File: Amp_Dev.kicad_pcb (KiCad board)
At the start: 2 copper layers, 100 x 100 mm, 39 parts, among them J1 SMA, J10 SMA, J11 CONN_01X02, Q1 DMN2075U, U1 MML09211H, U4 SN74LVC1G17, U5 TLV702, U6 LTC2644

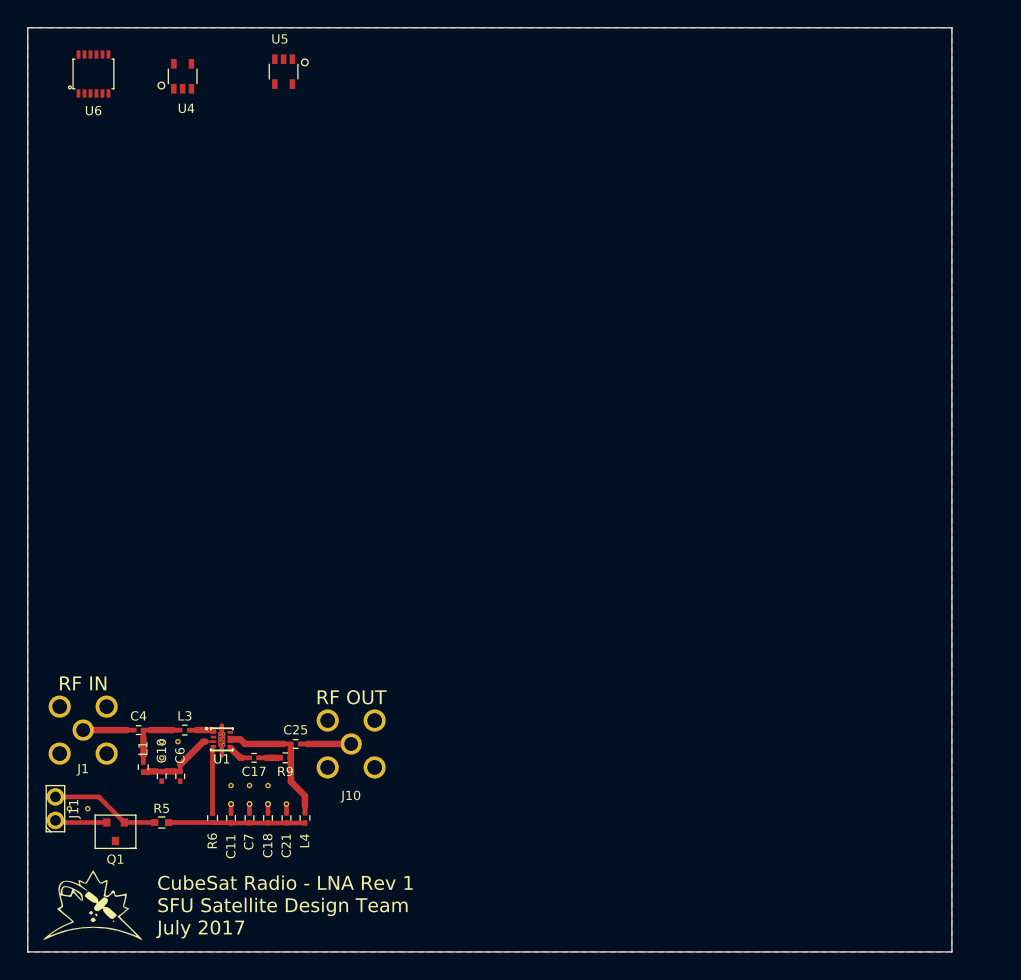
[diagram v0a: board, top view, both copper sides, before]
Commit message: Added diplexer board and other changes
-Adjusted RF track width to 0.6 mm from 0.7 mm
-Added diplexer board
-Added extra board cuts and mouse bites
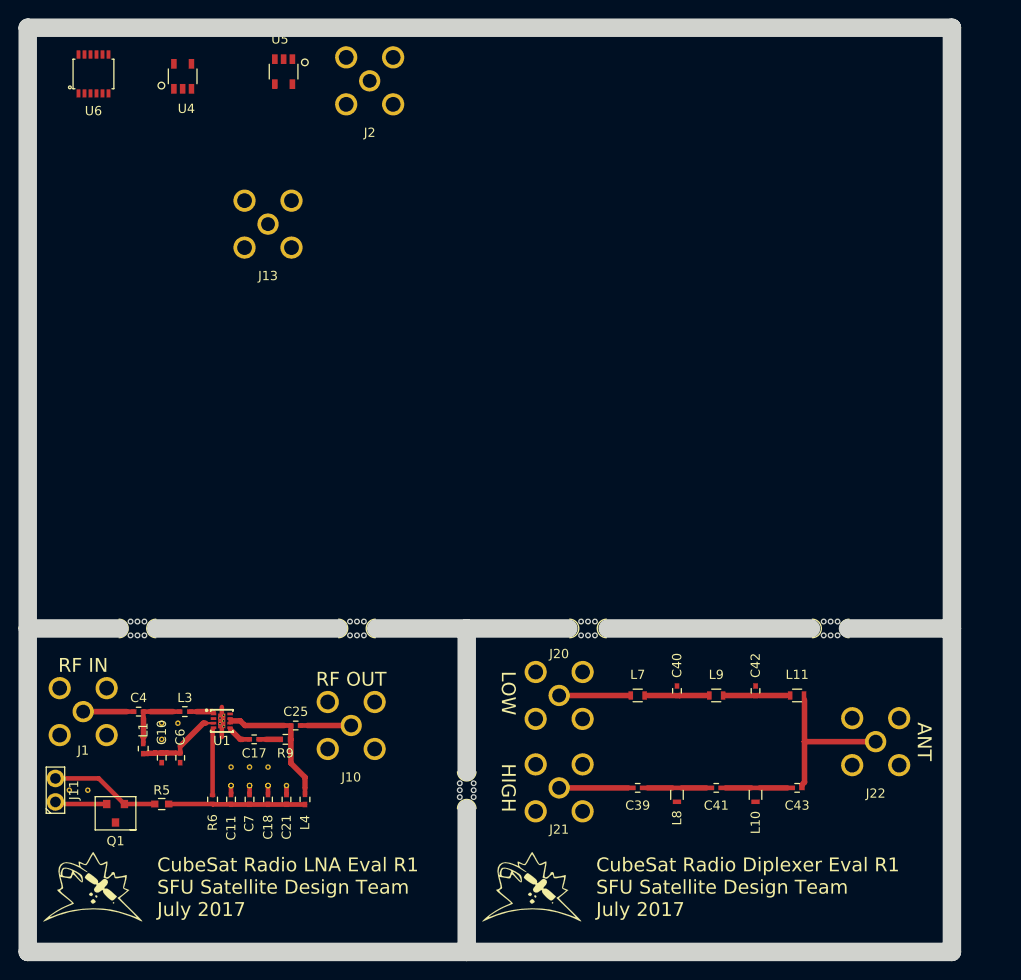
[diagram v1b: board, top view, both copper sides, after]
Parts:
- added C39: 8.2pF, SFUSat:C_0402, F.Cu at (166.0, 132.2)
- added C40: 8pF, SFUSat:C_0402, F.Cu at (170.2, 121.8)
- added C41: 3pF, SFUSat:C_0402, F.Cu at (174.5, 132.2)
- added C42: 10pF, SFUSat:C_0402, F.Cu at (178.8, 121.8)
- added C43: 3.3pF, SFUSat:C_0402, F.Cu at (183.2, 132.2)
- added G***: LOGO, SFUSat:SFUSat_15mm_2, F.Cu at (154.5, 143.0)
- added J13: SMA, SFUSat:SMA-Vert-TH, F.Cu at (126.0, 71.2)
- added J2: SMA, SFUSat:SMA-Vert-TH, F.Cu at (137.0, 55.8)
- added J20: SMA, SFUSat:SMA-Vert-TH, F.Cu at (157.5, 122.2)
- added J21: SMA, SFUSat:SMA-Vert-TH, F.Cu at (157.5, 132.2)
- added J22: SMA, SFUSat:SMA-Vert-TH, F.Cu at (191.8, 127.2)
- added L10: 7.5nH, SFUSat:L_0603, F.Cu at (178.8, 133.0)
- added L11: 22nH, SFUSat:L_0603, F.Cu at (183.2, 122.2)
- added L7: 8.7nH, SFUSat:L_0603, F.Cu at (166.0, 122.2)
- added L8: 9.5nH, SFUSat:L_0603, F.Cu at (170.2, 133.0)
- added L9: 24nH, SFUSat:L_0603, F.Cu at (174.5, 122.2)
- added mouse-bite-2mm-slot: VAL**, SFUSat:mouse-bite-2mm-slot, F.Cu at (135.6, 115.0)
- added mouse-bite-2mm-slot: VAL**, SFUSat:mouse-bite-2mm-slot, F.Cu at (147.5, 132.5)
- added mouse-bite-2mm-slot: VAL**, SFUSat:mouse-bite-2mm-slot, F.Cu at (111.9, 115.0)
- added mouse-bite-2mm-slot: VAL**, SFUSat:mouse-bite-2mm-slot, F.Cu at (186.9, 115.0)
- added mouse-bite-2mm-slot: VAL**, SFUSat:mouse-bite-2mm-slot, F.Cu at (160.6, 115.0)
- moved C10 2.00 mm to (114.5, 129.0)
- moved C11 2.00 mm to (122.0, 133.5)
- moved C17 2.00 mm to (124.5, 127.0)
- moved C18 2.00 mm to (126.0, 133.5)
- moved C21 2.00 mm to (128.0, 133.5)
- moved C25 2.00 mm to (129.0, 125.5)
- moved C4 2.00 mm to (112.0, 124.0)
- moved C6 2.00 mm to (116.5, 129.0)
- moved C7 2.00 mm to (124.0, 133.5)
- moved G*** 2.00 mm to (107.0, 143.0)
- moved J1 2.00 mm to (106.0, 124.0)
- moved J10 2.00 mm to (135.0, 125.5)
- moved J11 2.00 mm to (103.0, 132.5)
- moved L1 2.00 mm to (112.5, 128.0)
- moved L3 2.00 mm to (117.0, 124.0)
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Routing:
- net Net-(C43-Pad1): track 0.00 -> 18.1 mm
- net Net-(C39-Pad2): track 0.00 -> 7.97 mm
- net Net-(J20-Pad1): track 0.00 -> 7.75 mm
- net Net-(C41-Pad1): track 0.00 -> 7.70 mm
- net Net-(C39-Pad1): track 0.00 -> 7.45 mm
- net Net-(C42-Pad1): track 0.00 -> 7.27 mm
- net Net-(C40-Pad1): track 0.00 -> 7.06 mm
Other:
- outline, holes or cut-outs redrawn
- net class RF: trace_width 0.7 -> 0.6
- board text added: "ANT"
- board text added: "CubeSat Radio Diplexer Eval R1 SFU Satellite Design Team July 2017"
- board text added: "CubeSat Radio LNA Eval R1 SFU Satellite Design Team July 2017"
- board text added: "HIGH"
- board text added: "LOW"
- board text removed: "CubeSat Radio - LNA Rev 1 SFU Satellite Design Team July 2017"

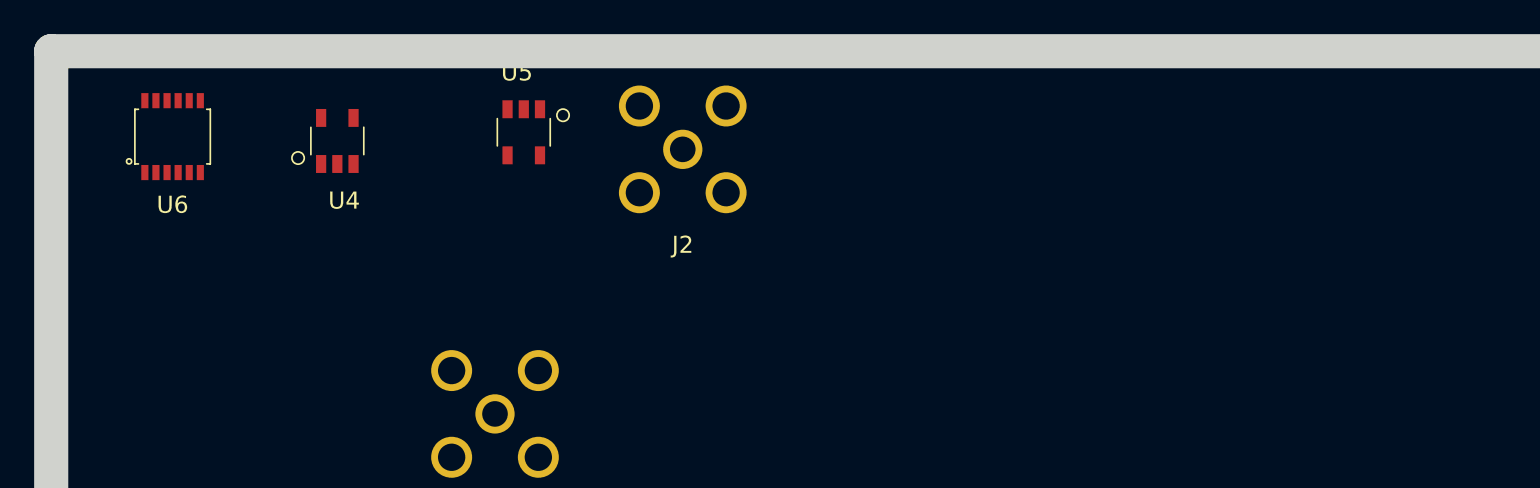
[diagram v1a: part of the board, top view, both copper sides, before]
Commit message: Further schematic updates
-Added more component footprints
-Forward annotated new components to PCB
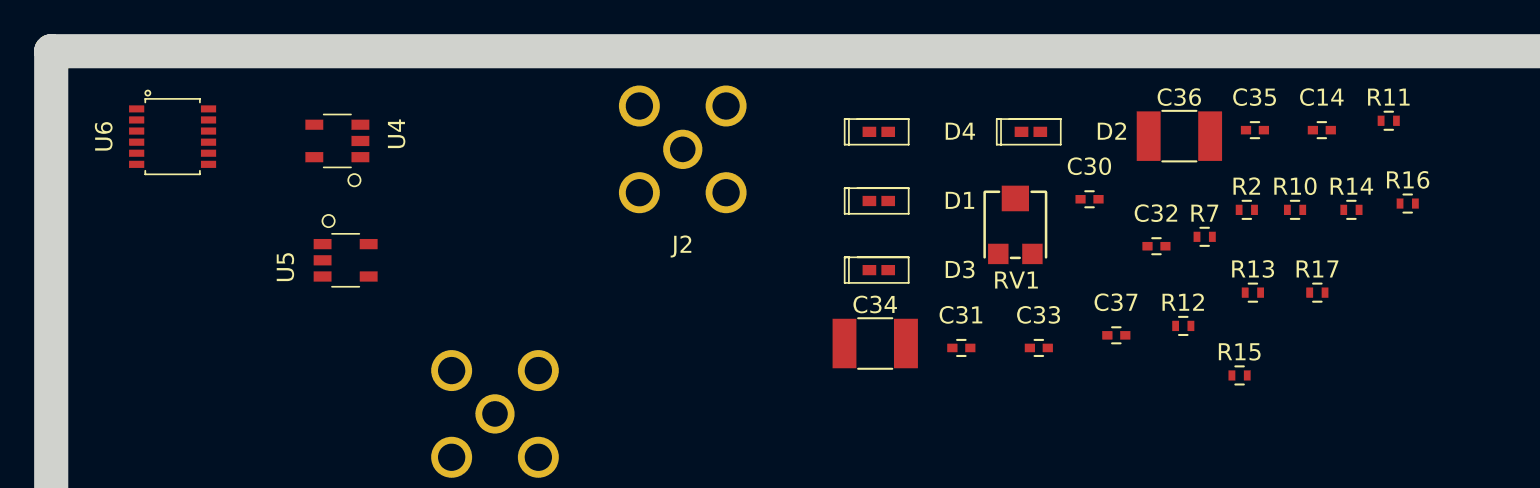
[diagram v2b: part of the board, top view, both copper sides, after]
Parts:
- added C14: 0.1uF, SFUSat:C_0402, F.Cu at (174.4, 54.6)
- added C30: 0.1uF, SFUSat:C_0402, F.Cu at (160.8, 58.7)
- added C31: 0.1uF, SFUSat:C_0402, F.Cu at (153.3, 67.4)
- added C32: 1uF, SFUSat:C_0402, F.Cu at (164.8, 61.4)
- added C33: 0.1uF, SFUSat:C_0402, F.Cu at (157.9, 67.4)
- added C34: 10uF, SFUSat:C_1210, F.Cu at (148.3, 67.1)
- added C35: 1uF, SFUSat:C_0402, F.Cu at (170.5, 54.6)
- added C36: 10uF, SFUSat:C_1210, F.Cu at (166.1, 55.0)
- added C37: 0.1uF, SFUSat:C_0402, F.Cu at (162.4, 66.6)
- added D1: PESD5Zx, SFUSat:PESD57zx, F.Cu at (148.5, 58.8)
- added D2: PESD5Zx, SFUSat:PESD57zx, F.Cu at (157.4, 54.7)
- added D3: PESD5Zx, SFUSat:PESD57zx, F.Cu at (148.5, 62.8)
- added D4: PESD5Zx, SFUSat:PESD57zx, F.Cu at (148.5, 54.7)
- added R10: 10K, SFUSat:R_0402, F.Cu at (172.9, 59.3)
- added R11: 10K, SFUSat:R_0402, F.Cu at (178.4, 54.1)
- added R12: 10K, SFUSat:R_0402, F.Cu at (166.3, 66.1)
- added R13: 10K, SFUSat:R_0402, F.Cu at (170.4, 64.1)
- added R14: 1K, SFUSat:R_0402, F.Cu at (176.2, 59.3)
- added R15: 1k, SFUSat:R_0402, F.Cu at (169.6, 69.0)
- added R16: 1k, SFUSat:R_0402, F.Cu at (179.5, 58.9)
- added R17: 287R, SFUSat:R_0402, F.Cu at (174.2, 64.1)
- added R2: 1K, SFUSat:R_0402, F.Cu at (170.0, 59.3)
- added R7: 1K, SFUSat:R_0402, F.Cu at (167.6, 60.9)
- added RV1: POT, SFUSat:TC33_SMD, F.Cu at (156.5, 60.1)
- moved U5 12.9 mm to (117.2, 62.2), turned to 270 degrees
- turned U4 to 90 degrees
- turned U6 to 270 degrees

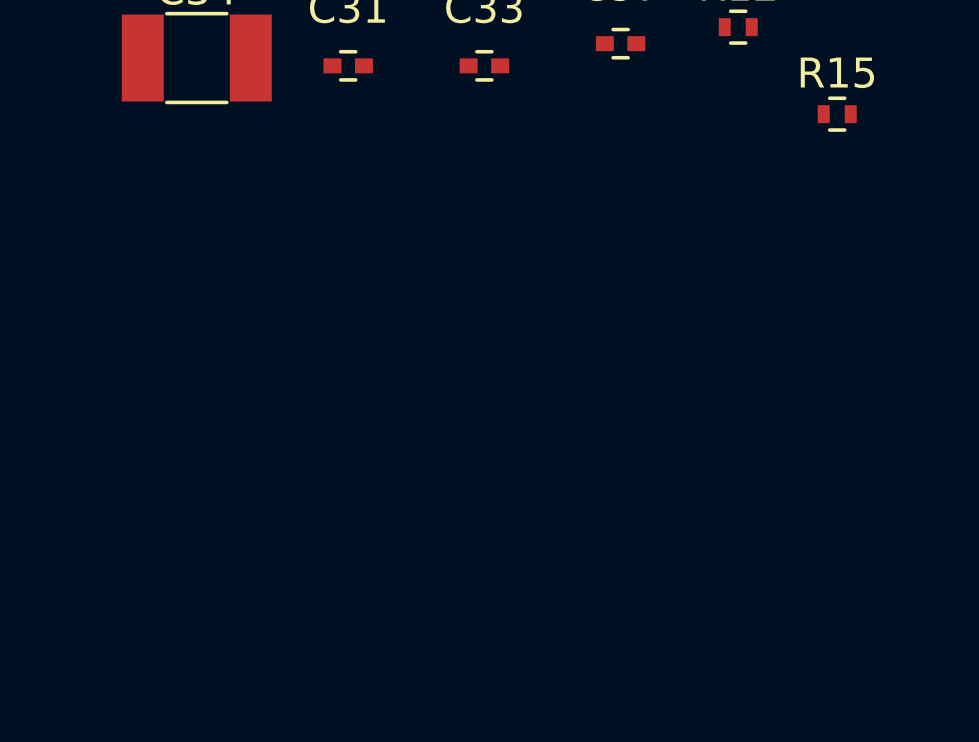
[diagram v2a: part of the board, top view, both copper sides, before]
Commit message: Added powerand output power control circuitry to sch and layout
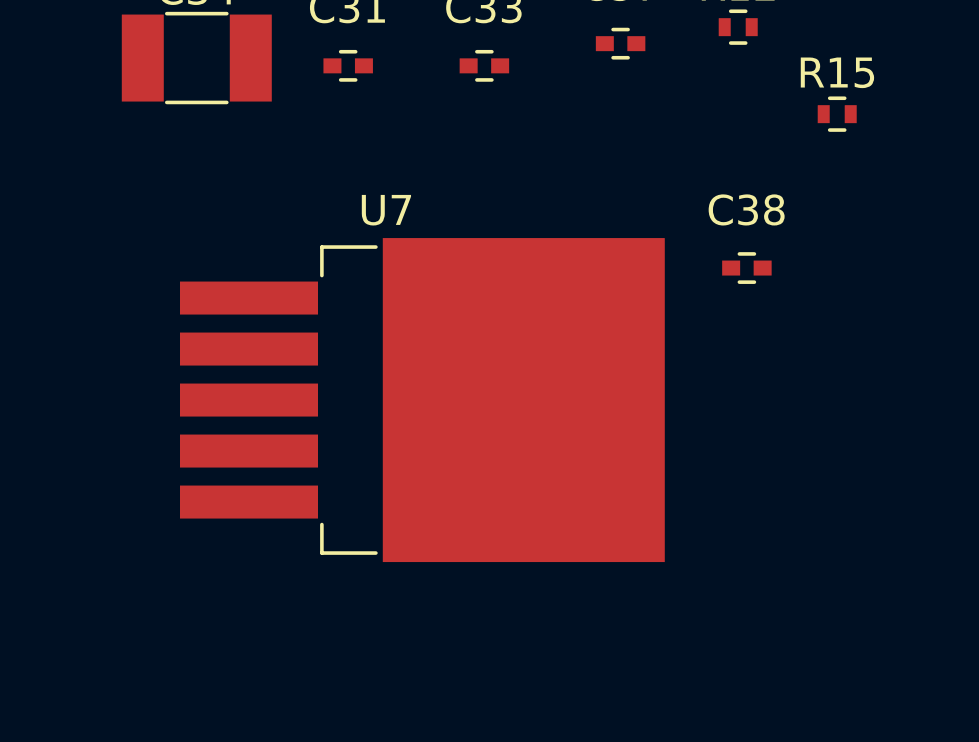
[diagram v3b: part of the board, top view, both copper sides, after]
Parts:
- added C38: 0.1uF, SFUSat:C_0402, F.Cu at (166.6, 74.1)
- added U7: RT9183, SFUSat:TO-263-5Lead, F.Cu at (154.6, 78.5)
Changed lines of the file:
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@@
 (kicad_pcb (version 4) (host pcbnew 4.0.5)
   (general
-    (links 142)
-    (no_connects 35)
+    (links 154)
+    (no_connects 40)
     (area 98.999999 48.999999 201.000001 151.000001)
     (thickness 0.6)
@@
     (tracks 115)
     (zones 0)
-    (modules 84)
+    (modules 86)
     (nets 49)
   )
@@
       (net 48 /3.1V) (solder_paste_margin -0.05))
   )
+  (module SFUSat:C_0402 (layer F.Cu)
+    (at 166.611428 74.125)
+    (descr "Capacitor SMD 0402, reflow soldering, AVX (see smccp.pdf)")
+    (tags "capacitor 0402")
+    (attr smd)
+    (fp_text reference C38 (at 0 -1.9) (layer F.SilkS)
+      (effects (font (size 1 1) (thickness 0.15)))
+    )
+    (fp_text value 0.1uF (at 0 1.27) (layer F.Fab)
+      (effects (font (size 1 1) (thickness 0.15)))
+    )
+    (fp_text user %R (at 0 -1.9) (layer F.Fab)
+      (effects (font (size 1 1) (thickness 0.15)))
+    )
+    (fp_line (start -0.5 0.25) (end -0.5 -0.25) (layer F.Fab) (width 0.1))
+    (fp_line (start 0.5 0.25) (end -0.5 0.25) (layer F.Fab) (width 0.1))
+    (fp_line (start 0.5 -0.25) (end 0.5 0.25) (layer F.Fab) (width 0.1))
+    (fp_line (start -0.5 -0.25) (end 0.5 -0.25) (layer F.Fab) (width 0.1))
+    (fp_line (start 0.25 -0.47) (end -0.25 -0.47) (layer F.SilkS) (width 0.12))
+    (fp_line (start -0.25 0.47) (end 0.25 0.47) (layer F.SilkS) (width 0.12))
+    (fp_line (start -1 -0.4) (end 1 -0.4) (layer F.CrtYd) (width 0.05))
+    (fp_line (start -1 -0.4) (end -1 0.4) (layer F.CrtYd) (width 0.05))
+    (fp_line (start 1 0.4) (end 1 -0.4) (layer F.CrtYd) (width 0.05))
+    (fp_line (start 1 0.4) (end -1 0.4) (layer F.CrtYd) (width 0.05))
+    (pad 1 smd rect (at -0.525 0) (size 0.6 0.5) (layers F.Cu F.Paste F.Mask)
+      (net 22 /3V1) (solder_paste_margin -0.05))
+    (pad 2 smd rect (at 0.525 0) (size 0.6 0.5) (layers F.Cu F.Paste F.Mask)
+      (net 4 GND) (solder_paste_margin -0.05))
+    (model Capacitors_SMD.3dshapes/C_0402.wrl
+      (at (xyz 0 0 0))
+      (scale (xyz 1 1 1))
+      (rotate (xyz 0 0 0))
+    )
+  )
+  (module SFUSat:TO-263-5Lead (layer F.Cu)
+    (at 154.595001 78.525)
+    (descr "D2PAK / TO-263 3-lead smd package")
+    (tags "D2PAK D2PAK-3 TO-263AB TO-263")
+    (attr smd)
+    (fp_text reference U7 (at 0 -6.3 180) (layer F.SilkS)
+      (effects (font (size 1 1) (thickness 0.15)))
+    )
+    (fp_text value RT9183 (at 0 6.45 180) (layer F.Fab)
+      (effects (font (size 1 1) (thickness 0.15)))
+    )
+    (fp_line (start -2.15 -5.1) (end -2.15 -4.15) (layer F.SilkS) (width 0.12))
+    (fp_line (start -2.15 5.1) (end -2.15 4.15) (layer F.SilkS) (width 0.12))
+    (fp_line (start 9.52 5.65) (end -7.12 5.65) (layer F.CrtYd) (width 0.05))
+    (fp_line (start 9.52 -5.65) (end 9.52 5.65) (layer F.CrtYd) (width 0.05))
+    (fp_line (start 9.52 -5.65) (end -7.12 -5.65) (layer F.CrtYd) (width 0.05))
+    (fp_line (start -7.12 -5.65) (end -7.12 5.65) (layer F.CrtYd) (width 0.05))
+    (fp_line (start -2.15 5.1) (end -0.35 5.1) (layer F.SilkS) (width 0.12))
+    (fp_line (start -0.35 -5.1) (end -2.15 -5.1) (layer F.SilkS) (width 0.12))
+    (fp_line (start 6.95 5) (end 8.15 5) (layer F.Fab) (width 0.1))
+    (fp_line (start 8.15 5) (end 8.15 -5) (layer F.Fab) (width 0.1))
+    (fp_line (start 8.15 -5) (end 6.95 -5) (layer F.Fab) (width 0.1))
+    (fp_line (start -2.05 -5) (end -2.05 5) (layer F.Fab) (width 0.1))
+    (fp_line (start -2.05 5) (end 6.95 5) (layer F.Fab) (width 0.1))
+    (fp_line (start 6.95 5) (end 6.95 -5) (layer F.Fab) (width 0.1))
+    (fp_line (start 6.95 -5) (end -2.05 -5) (layer F.Fab) (width 0.1))
+    (pad 3 smd rect (at 7.15 2.98) (size 4 4.5) (layers F.Cu F.Paste F.Mask)
+      (net 4 GND))
+    (pad 3 smd rect (at 2 2.92) (size 4 4.5) (layers F.Cu F.Paste F.Mask)
+      (net 4 GND))
+    (pad 3 smd rect (at 7.11 -2.99) (size 4 4.5) (layers F.Cu F.Paste F.Mask)
+      (net 4 GND))
+    (pad 5 smd rect (at -4.58 3.4) (size 4.6 1.1) (layers F.Cu F.Paste F.Mask)
+      (net 46 "Net-(R16-Pad2)") (solder_paste_margin -0.05))
+    (pad 4 smd rect (at -4.58 1.7) (size 4.6 1.1) (layers F.Cu F.Paste F.Mask)
+      (net 37 "Net-(C36-Pad1)") (solder_paste_margin -0.05))
+    (pad 2 smd rect (at -4.58 -1.7) (size 4.6 1.1) (layers F.Cu F.Paste F.Mask)
+      (net 36 "Net-(C33-Pad1)") (solder_paste_margin -0.05))
+    (pad 3 smd rect (at 4.58 0) (size 9.4 10.8) (layers F.Cu F.Mask)
+      (net 4 GND))
+    (pad 3 smd rect (at -4.58 0) (size 4.6 1.1) (layers F.Cu F.Paste F.Mask)
+      (net 4 GND) (solder_paste_margin -0.05))
+    (pad 1 smd rect (at -4.58 -3.4) (size 4.6 1.1) (layers F.Cu F.Paste F.Mask)
+      (net 45 "Net-(R15-Pad2)") (solder_paste_margin -0.05))
+    (pad 3 smd rect (at 2.05 -3) (size 4 4.5) (layers F.Cu F.Paste F.Mask)
+      (net 4 GND))
+    (model TO_SOT_Packages_SMD.3dshapes/TO-263-5Lead.wrl
+      (at (xyz -0.18 0 0))
+      (scale (xyz 1 1 1))
+      (rotate (xyz 0 0 90))
+    )
+  )
   (gr_line (start 188.75 115) (end 200 115) (angle 90) (layer Edge.Cuts) (width 2))
